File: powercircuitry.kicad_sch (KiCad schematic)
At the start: 163 parts, among them U1002 AM6231ASGGGAALW, U3001 TPS6521903RHBR, U3002 TLV62595DMQR

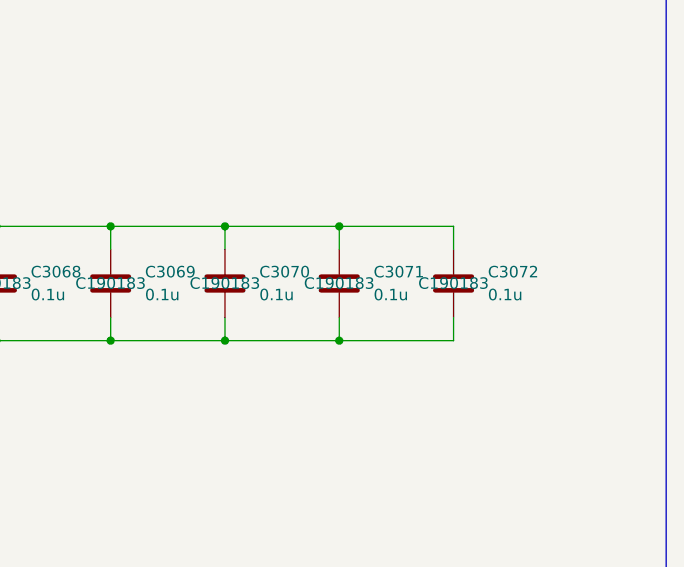
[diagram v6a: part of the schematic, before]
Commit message: Finished routing Rev B and fixed all errors and warnings
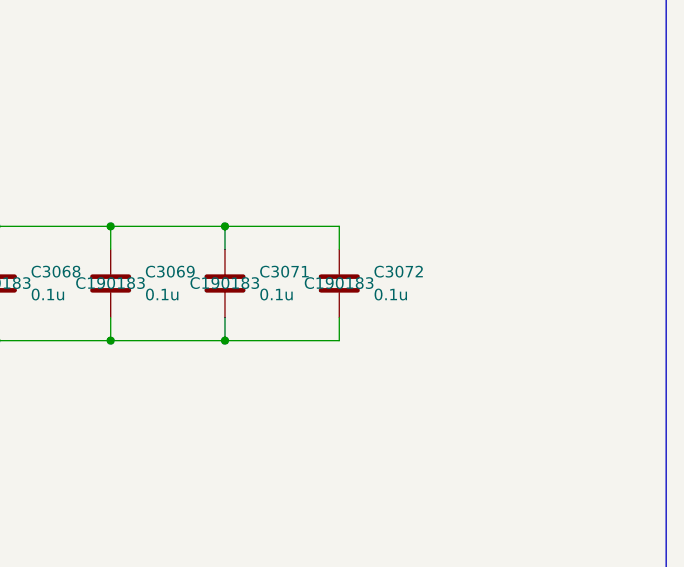
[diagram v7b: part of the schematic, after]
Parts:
- removed C3070: 0.1u, Capacitor_SMD:C_0201_0603Metric, symbol Device:C
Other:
- moved on the sheet: C3071, C3072
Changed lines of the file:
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@@
 	)
 	(junction
-		(at 632.46 444.5)
-		(diameter 0)
-		(color 0 0 0 0)
-	)
-	(junction
 		(at 521.97 558.8)
 		(diameter 0)
@@
 	)
 	(junction
+		(at 632.46 431.8)
+		(diameter 0)
+		(color 0 0 0 0)
+	)
+	(junction
 		(at 521.97 617.22)
 		(diameter 0)
@@
 	)
 	(junction
-		(at 645.16 444.5)
-		(diameter 0)
-		(color 0 0 0 0)
-	)
-	(junction
 		(at 477.52 334.01)
 		(diameter 0)
@@
 	)
 	(junction
+		(at 632.46 444.5)
+		(diameter 0)
+		(color 0 0 0 0)
+	)
+	(junction
 		(at 424.18 156.21)
 		(diameter 0)
@@
 	)
 	(junction
-		(at 632.46 431.8)
-		(diameter 0)
-		(color 0 0 0 0)
-	)
-	(junction
 		(at 426.72 607.06)
 		(diameter 0)
@@
 	)
 	(junction
-		(at 645.16 431.8)
-		(diameter 0)
-		(color 0 0 0 0)
-	)
-	(junction
 		(at 416.56 397.51)
 		(diameter 0)
@@
 	(wire
 		(pts
-			(xy 632.46 431.8) (xy 632.46 434.34)
-		)
-		(stroke
-			(width 0)
-			(type default)
-		)
-	)
-	(wire
-		(pts
 			(xy 528.32 478.79) (xy 528.32 476.25)
 		)
@@
 	(wire
 		(pts
-			(xy 645.16 431.8) (xy 645.16 434.34)
+			(xy 632.46 431.8) (xy 632.46 434.34)
 		)
 		(stroke
@@
 	(wire
 		(pts
-			(xy 632.46 444.5) (xy 632.46 441.96)
-		)
-		(stroke
-			(width 0)
-			(type default)
-		)
-	)
-	(wire
-		(pts
 			(xy 528.32 306.07) (xy 537.21 306.07)
 		)
@@
 	(wire
 		(pts
-			(xy 632.46 431.8) (xy 645.16 431.8)
-		)
-		(stroke
-			(width 0)
-			(type default)
-		)
-	)
-	(wire
-		(pts
 			(xy 424.18 151.13) (xy 424.18 153.67)
 		)
@@
 	(wire
 		(pts
-			(xy 645.16 444.5) (xy 645.16 441.96)
+			(xy 632.46 444.5) (xy 632.46 441.96)
 		)
 		(stroke
@@
 	(wire
 		(pts
-			(xy 645.16 431.8) (xy 657.86 431.8)
+			(xy 632.46 431.8) (xy 645.16 431.8)
 		)
 		(stroke
@@
 	(wire
 		(pts
-			(xy 657.86 431.8) (xy 657.86 434.34)
+			(xy 645.16 431.8) (xy 645.16 434.34)
 		)
 		(stroke
@@
 	(wire
 		(pts
-			(xy 632.46 444.5) (xy 645.16 444.5)
-		)
-		(stroke
-			(width 0)
-			(type default)
-		)
-	)
-	(wire
-		(pts
 			(xy 365.76 431.8) (xy 378.46 431.8)
 		)
@@
 	(wire
 		(pts
-			(xy 657.86 444.5) (xy 657.86 441.96)
+			(xy 645.16 444.5) (xy 645.16 441.96)
 		)
 		(stroke
@@
 	(wire
 		(pts
-			(xy 645.16 444.5) (xy 657.86 444.5)
+			(xy 632.46 444.5) (xy 645.16 444.5)
 		)
 		(stroke
@@
 	(symbol
 		(lib_id "Device:C")
-		(at 657.86 438.15 0)
+		(at 645.16 438.15 0)
 		(unit 1)
 		(exclude_from_sim no)
@@
 		(fields_autoplaced yes)
 		(property "Reference" "C3072"
-			(at 661.67 436.8799 0)
+			(at 648.97 436.8799 0)
 			(effects
 				(font
@@
 		)
 		(property "Value" "0.1u"
-			(at 661.67 439.4199 0)
+			(at 648.97 439.4199 0)
 			(effects
 				(font
@@
 		)
 		(property "Footprint" "Capacitor_SMD:C_0201_0603Metric"
-			(at 658.8252 441.96 0)
+			(at 646.1252 441.96 0)
 			(effects
 				(font
@@
 		)
 		(property "Datasheet" "~"
-			(at 657.86 438.15 0)
+			(at 645.16 438.15 0)
 			(effects
 				(font
@@
 		)
 		(property "Description" "Unpolarized capacitor"
-			(at 657.86 438.15 0)
+			(at 645.16 438.15 0)
 			(effects
 				(font
@@
 		)
 		(property "JLCPCB Part#" "C190183"
-			(at 657.86 438.15 0)
+			(at 645.16 438.15 0)
 			(effects
 				(font
@@
 	)
 	(symbol
-		(lib_id "Device:C")
-		(at 632.46 438.15 0)
-		(unit 1)
-		(exclude_from_sim no)
-		(in_bom yes)
-		(on_board yes)
-		(dnp no)
-		(fields_autoplaced yes)
-		(property "Reference" "C3070"
-			(at 636.27 436.8799 0)
-			(effects
-				(font
-					(size 1.27 1.27)
-				)
-				(justify left)
-			)
-		)
-		(property "Value" "0.1u"
-			(at 636.27 439.4199 0)
-			(effects
-				(font
-					(size 1.27 1.27)
-				)
-				(justify left)
-			)
-		)
-		(property "Footprint" "Capacitor_SMD:C_0201_0603Metric"
-			(at 633.4252 441.96 0)
-			(effects
-				(font
-					(size 1.27 1.27)
-				)
-				(hide yes)
-			)
-		)
-		(property "Datasheet" "~"
-			(at 632.46 438.15 0)
-			(effects
-				(font
-					(size 1.27 1.27)
-				)
-				(hide yes)
-			)
-		)
-		(property "Description" "Unpolarized capacitor"
-			(at 632.46 438.15 0)
-			(effects
-				(font
-					(size 1.27 1.27)
-				)
-				(hide yes)
-			)
-		)
-		(property "JLCPCB Part#" "C190183"
-			(at 632.46 438.15 0)
-			(effects
-				(font
-					(size 1.27 1.27)
-				)
-			)
-		)
-		(pin "1"
-		)
-		(pin "2"
-		)
-		(instances
-			(project "Leonhart"
-				(path "/b43b7bca-e50d-42ec-8ff0-e0016dfefe0a/13a7821e-2ee3-4360-911d-96166c961e5a"
-					(reference "C3070")
-					(unit 1)
-				)
-			)
-		)
-	)
-	(symbol
 		(lib_id "power:VDD")
 		(at 238.76 196.85 0)
@@
 	(symbol
 		(lib_id "Device:C")
-		(at 645.16 438.15 0)
+		(at 632.46 438.15 0)
 		(unit 1)
 		(exclude_from_sim no)
@@
 		(fields_autoplaced yes)
 		(property "Reference" "C3071"
-			(at 648.97 436.8799 0)
+			(at 636.27 436.8799 0)
 			(effects
 				(font
@@
 		)
 		(property "Value" "0.1u"
-			(at 648.97 439.4199 0)
+			(at 636.27 439.4199 0)
 			(effects
 				(font
@@
 		)
 		(property "Footprint" "Capacitor_SMD:C_0201_0603Metric"
-			(at 646.1252 441.96 0)
+			(at 633.4252 441.96 0)
 			(effects
 				(font
@@
 		)
 		(property "Datasheet" "~"
-			(at 645.16 438.15 0)
+			(at 632.46 438.15 0)
 			(effects
 				(font
@@
 		)
 		(property "Description" "Unpolarized capacitor"
-			(at 645.16 438.15 0)
+			(at 632.46 438.15 0)
 			(effects
 				(font
@@
 		)
 		(property "JLCPCB Part#" "C190183"
-			(at 645.16 438.15 0)
+			(at 632.46 438.15 0)
 			(effects
 				(font

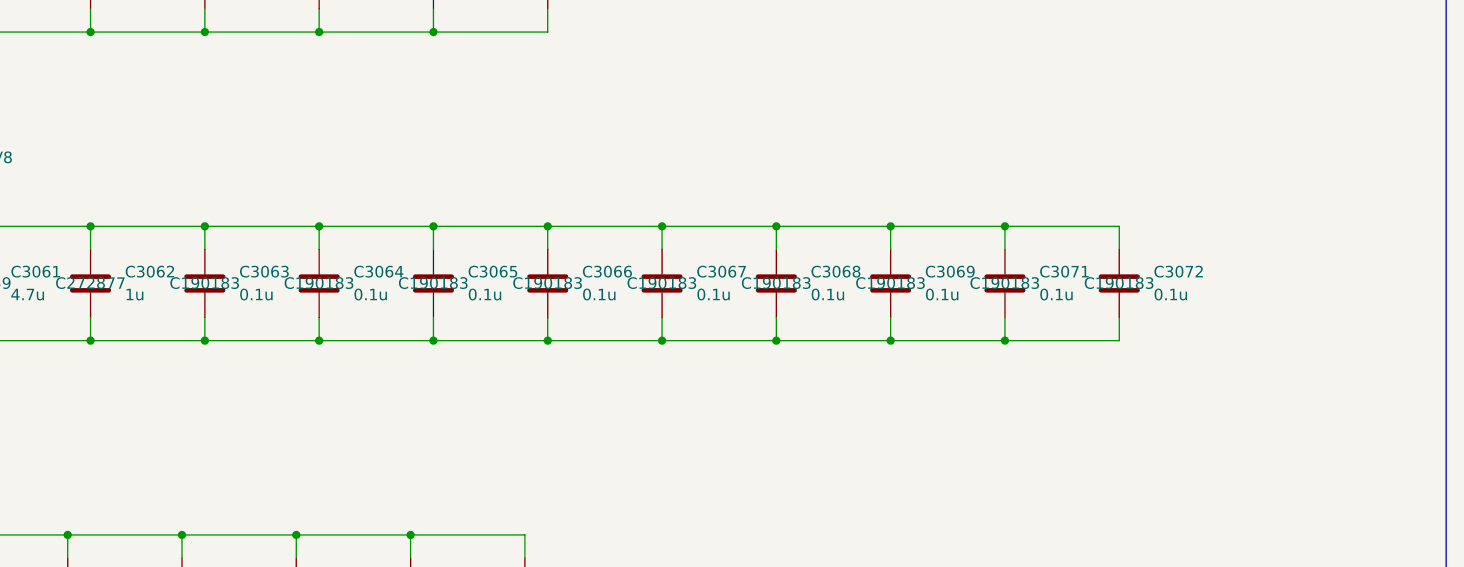
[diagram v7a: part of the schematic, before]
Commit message: Fixed Ethernet inductor and capacitor regulator parts. Cleaned up Ethernet routing
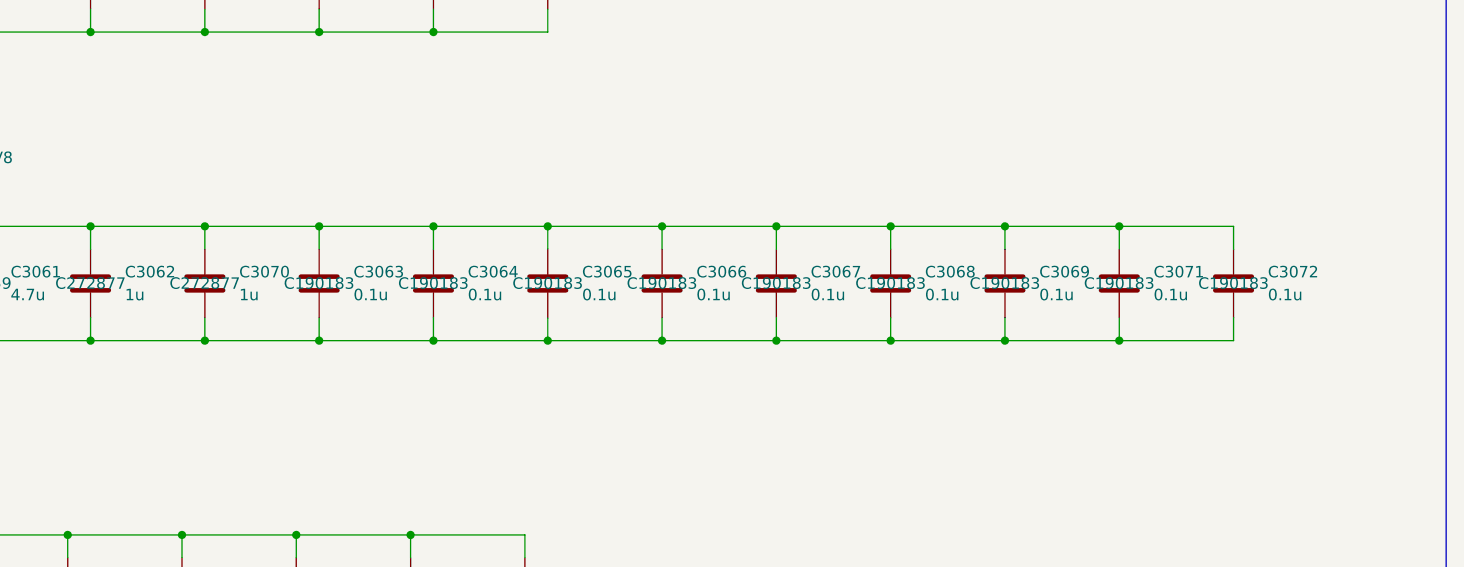
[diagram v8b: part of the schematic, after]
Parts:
- added C3070: 1u, Capacitor_SMD:C_0201_0603Metric, symbol Device:C
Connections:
- net GND: now also C3070.2
- net VDD_1V8: now also C3070.1
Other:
- moved on the sheet: C3063, C3064, C3065, C3066, C3067, C3068, C3069, C3071, C3072
